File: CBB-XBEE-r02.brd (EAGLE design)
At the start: 86.4 x 54.6 mm, 35 parts, among them IC1 TLV1117-XX, J1 HEADER_1X23, J10 HEADER_1X9, J11 HEADER_1X9, J12 HEADER_1X1, J13 HEADER_1X1, J14 HEADER_1X2, J15 HEADER_1X1, J16 HEADER_1X1, J17 HEADER_1X1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

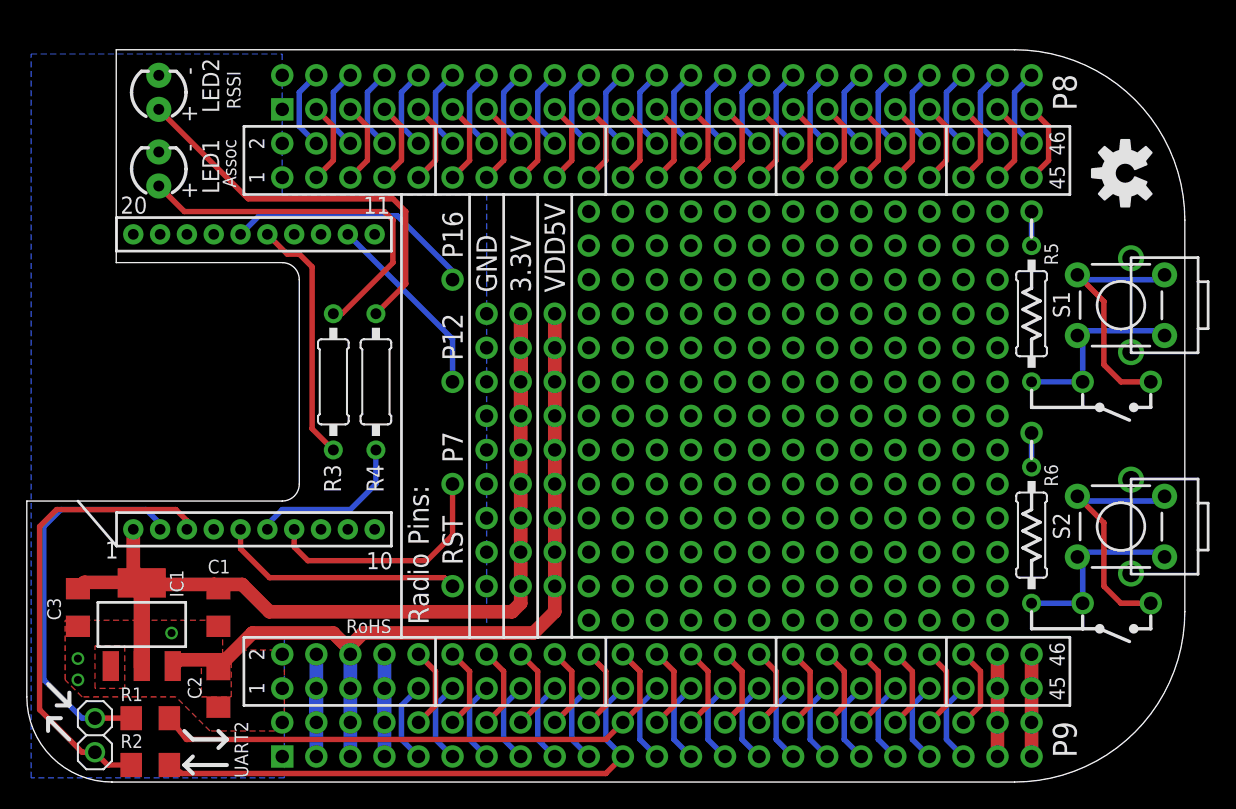
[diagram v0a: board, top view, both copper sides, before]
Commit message: modified layout to include extra test points for series 3 xbees.
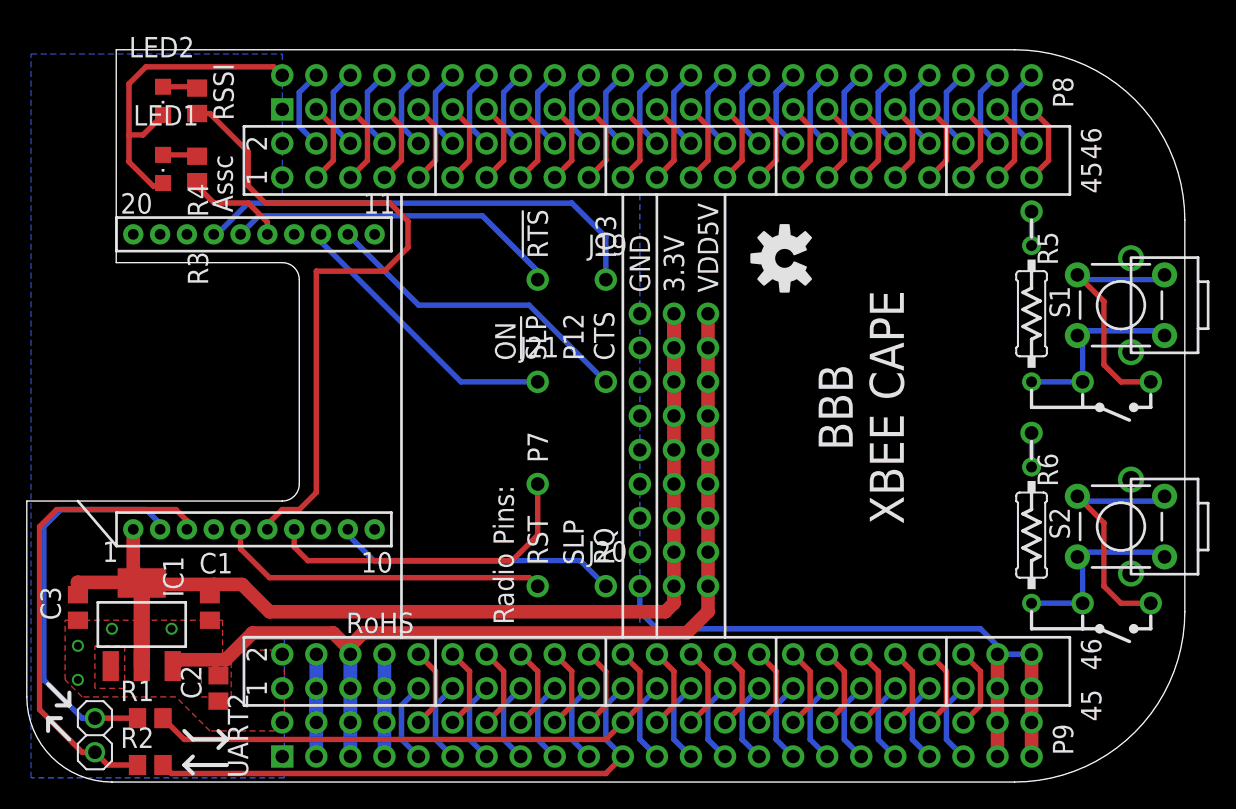
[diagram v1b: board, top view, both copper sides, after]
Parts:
- added J19, J20, J21: HEADER_1X1, logic-supply:HEADER_1X1
- C1, C2, C3: device logic-supply:C1206 -> logic-supply:C0805
- LED1, LED2: device SparkFun-LED:LED3MM -> adafruit:CHIPLED_0805
- R1, R2: device logic-supply:R1206 -> logic-supply:R0805
- R3, R4: device logic-supply:0207/10 -> logic-supply:R0805
- moved U$7 26.2 mm to (56.5, 39.1)
- moved R4 24.8 mm to (12.7, 50.8)
- moved R3 18.8 mm to (12.7, 45.7)
- moved J10 11.4 mm to (48.3, 14.6)
- moved J11 11.4 mm to (50.8, 14.6)
- moved J17 11.4 mm to (43.2, 29.8)
- moved J9 11.4 mm to (45.7, 14.6)
- moved J15 6.35 mm to (38.1, 14.6)
- moved J16 6.35 mm to (38.1, 22.2)
- moved J18 6.35 mm to (38.1, 37.5)
- moved LED2 0.71 mm to (10.2, 50.8), turned to 180 degrees
- moved C1 0.63 mm to (13.7, 13.0)
- moved LED1 0.32 mm to (10.2, 45.7), turned to 180 degrees
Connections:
- net RADIO_P12 renamed CTS
- net RADIO_P16 renamed RTS
- new net DIO3: J19.1, RADIO1.17
- new net ON_!SLEEP: J21.1, RADIO1.13
- new net SLEEP_RQ: J20.1, RADIO1.9
- net GND: now also LED1.C, LED2.C; no longer LED1.K, LED2.K
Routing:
- net GND: track 15.2 -> 72.6 mm, vias 3 -> 4
- net N$34: track 12.2 -> 51.6 mm
- net DIO3: track 0.00 -> 34.4 mm
- net N$96: track 30.1 -> 2.58 mm
- net N$35: track 27.7 -> 2.58 mm
- net SLEEP_RQ: track 0.00 -> 21.2 mm
- net ON_!SLEEP: track 0.00 -> 21.0 mm
- net 3V3: track 75.0 -> 87.6 mm
- net 5V: track 62.7 -> 74.5 mm
- net N$13: track 18.6 -> 7.58 mm
- net CTS: track 14.2 -> 23.8 mm
- net RADIO_P7: track 18.1 -> 24.5 mm
- net RTS: track 18.7 -> 25.1 mm
- net RADIO_RST: track 18.4 -> 24.8 mm
- net UART2_TX: track 40.7 -> 41.2 mm
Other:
- board text added: "!RTS"
- board text added: "Assc"
- board text added: "BBB XBEE CAPE"
- board text added: "IO3"
- board text added: "ON !SLP"
- board text added: "P12 CTS"
- board text added: "SLP RQ"
- board text removed: "+"
- board text removed: "-"
- board text removed: "Assoc"
- board text removed: "P12"
- board text removed: "P16"
